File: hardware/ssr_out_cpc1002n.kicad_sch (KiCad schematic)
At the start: 2 parts, among them U8 CPC1002N

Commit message: finalize revision of schematic
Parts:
- renumbered R13 to R10, U8 to U7
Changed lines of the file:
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@@
 		(on_board yes)
 		(dnp no)
-		(property "Reference" "R13"
+		(property "Reference" "R10"
 			(at 107.95 99.06 90)
 			(effects
@@
 			(project "BREAD_Slice"
 				(path "/66043bca-a260-4915-9fce-8a51d324c687/19c2c951-cbc7-421d-b9f1-26fcd710db6e"
+					(reference "R13")
+					(unit 1)
+				)
+				(path "/66043bca-a260-4915-9fce-8a51d324c687/71019fd0-2a2f-4475-a8d4-6b7755247a80"
+					(reference "R12")
+					(unit 1)
+				)
+				(path "/66043bca-a260-4915-9fce-8a51d324c687/ebb8db09-fc2c-4cfe-9c1d-88f995e3634a"
 					(reference "R11")
 					(unit 1)
 				)
-				(path "/66043bca-a260-4915-9fce-8a51d324c687/71019fd0-2a2f-4475-a8d4-6b7755247a80"
+				(path "/66043bca-a260-4915-9fce-8a51d324c687/ed7833cb-3235-4c08-a5c0-99570f082658"
 					(reference "R10")
-					(unit 1)
-				)
-				(path "/66043bca-a260-4915-9fce-8a51d324c687/ebb8db09-fc2c-4cfe-9c1d-88f995e3634a"
-					(reference "R9")
-					(unit 1)
-				)
-				(path "/66043bca-a260-4915-9fce-8a51d324c687/ed7833cb-3235-4c08-a5c0-99570f082658"
-					(reference "R13")
 					(unit 1)
 				)
@@
 		(dnp no)
 		(fields_autoplaced yes)
-		(property "Reference" "U8"
+		(property "Reference" "U7"
 			(at 123.19 82.55 0)
 			(effects
@@
 			(project "BREAD_Slice"
 				(path "/66043bca-a260-4915-9fce-8a51d324c687/19c2c951-cbc7-421d-b9f1-26fcd710db6e"
+					(reference "U10")
+					(unit 1)
+				)
+				(path "/66043bca-a260-4915-9fce-8a51d324c687/71019fd0-2a2f-4475-a8d4-6b7755247a80"
 					(reference "U9")
 					(unit 1)
 				)
-				(path "/66043bca-a260-4915-9fce-8a51d324c687/71019fd0-2a2f-4475-a8d4-6b7755247a80"
+				(path "/66043bca-a260-4915-9fce-8a51d324c687/ebb8db09-fc2c-4cfe-9c1d-88f995e3634a"
+					(reference "U8")
+					(unit 1)
+				)
+				(path "/66043bca-a260-4915-9fce-8a51d324c687/ed7833cb-3235-4c08-a5c0-99570f082658"
 					(reference "U7")
 					(unit 1)
 				)
-				(path "/66043bca-a260-4915-9fce-8a51d324c687/ebb8db09-fc2c-4cfe-9c1d-88f995e3634a"
-					(reference "U6")
-					(unit 1)
-				)
-				(path "/66043bca-a260-4915-9fce-8a51d324c687/ed7833cb-3235-4c08-a5c0-99570f082658"
-					(reference "U8")
-					(unit 1)
-				)

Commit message: revision of symbol attachment and clear out old layout and start new; kml-custom to kmlib-local
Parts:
- renumbered U7 to U6
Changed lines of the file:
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@@
 		(dnp no)
 		(fields_autoplaced yes)
-		(property "Reference" "U7"
+		(property "Reference" "U6"
 			(at 123.19 82.55 0)
 			(effects
@@
 			(project "BREAD_Slice"
 				(path "/66043bca-a260-4915-9fce-8a51d324c687/19c2c951-cbc7-421d-b9f1-26fcd710db6e"
-					(reference "U10")
+					(reference "U9")
 					(unit 1)
 				)
 				(path "/66043bca-a260-4915-9fce-8a51d324c687/71019fd0-2a2f-4475-a8d4-6b7755247a80"
-					(reference "U9")
+					(reference "U8")
 					(unit 1)
 				)
 				(path "/66043bca-a260-4915-9fce-8a51d324c687/ebb8db09-fc2c-4cfe-9c1d-88f995e3634a"
-					(reference "U8")
+					(reference "U7")
 					(unit 1)
 				)
 				(path "/66043bca-a260-4915-9fce-8a51d324c687/ed7833cb-3235-4c08-a5c0-99570f082658"
-					(reference "U7")
+					(reference "U6")
 					(unit 1)
 				)

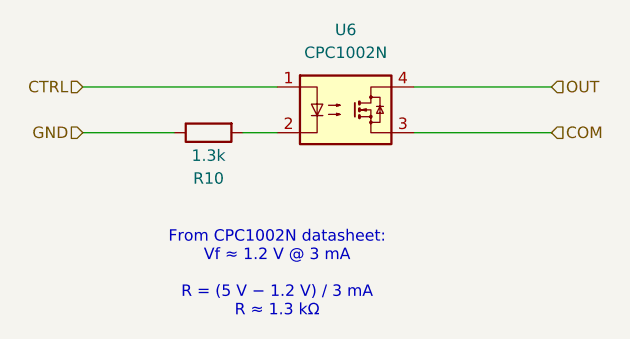
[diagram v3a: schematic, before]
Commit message: update all to KMLib, untrack backups in gitignore, and revise routing on board to simplify
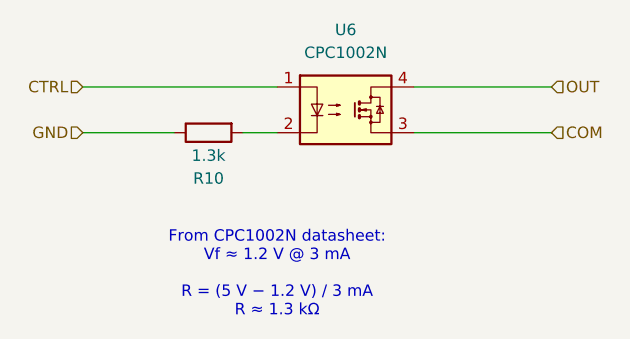
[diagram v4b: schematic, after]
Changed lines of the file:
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@@
 			)
 		)
-		(property "Datasheet" "https://www.littelfuse.com/assetdocs/littelfuse-integrated-circuits-cpc1002n-datasheet?assetguid=e3f473b5-dc7a-4246-906b-83ecf53ecf01"
+		(property "Datasheet" "http://www.ixysic.com/home/pdfs.nsf/www/CPC1002N.pdf/$file/CPC1002N.pdf"
 			(at 123.19 100.838 0)
 			(effects
@@
 			)
 		)
-		(property "Description" "Form A, Solid State Relay (Photo MOSFET) 60V, 0.7A, 0.55Ohm, DC, SOP-4"
+		(property "Description" "Form A, Solid State Relay (Photo MOSFET) 60V, 0.7A, 0.55Ohm, SOP-4"
 			(at 123.19 98.806 0)
 			(effects
